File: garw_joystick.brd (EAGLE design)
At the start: 45 x 30 mm, 15 parts, among them IC1 TLC339D, X1 PS-05_WL, X2 PS-08_WL

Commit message: Improve board
Signed-off-by: Ralf Ramsauer <ralf@vmexit.de>
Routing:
- net GARW4: track 35.6 -> 37.9 mm
- net GND: track 84.9 -> 85.5 mm

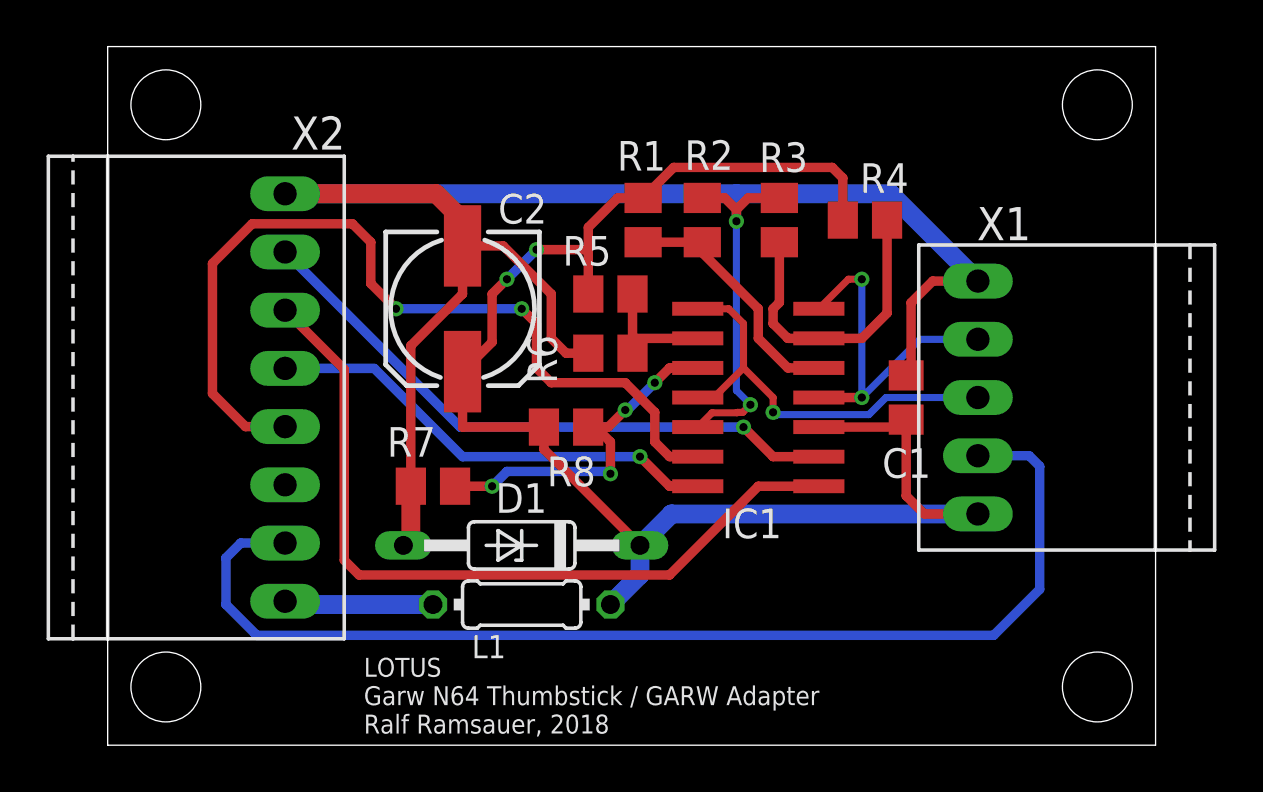
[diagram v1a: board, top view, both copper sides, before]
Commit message: Add low pass filters
Signed-off-by: Ralf Ramsauer <ralf@vmexit.de>
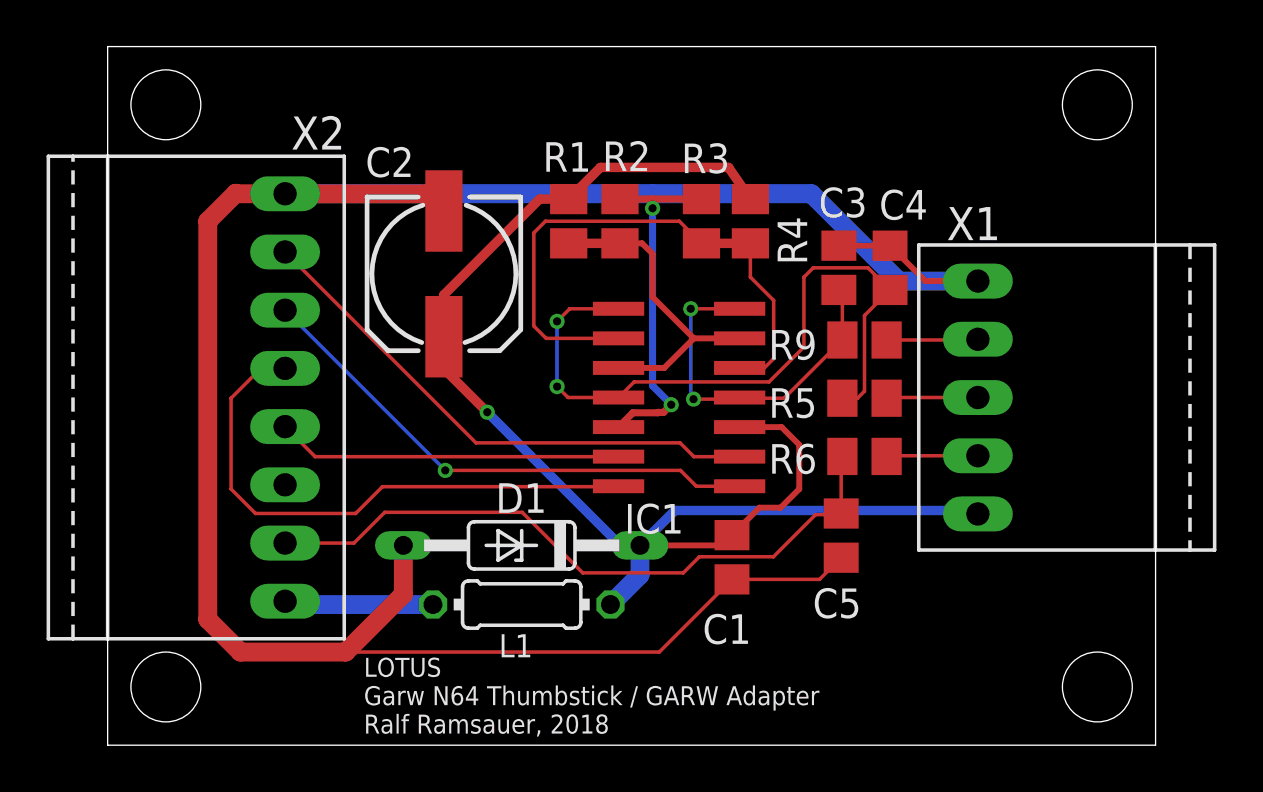
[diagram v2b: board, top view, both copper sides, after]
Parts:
- removed R7, R8: (no value), rcl:M0805
- added C3, C4, C5: 100n, rcl:C0805
- added R9: (no value), rcl:M0805
- R1, R3: value (none) -> 1k3
- R2, R4: value (none) -> 22k
- R6: value (none) -> 10k
- moved R5 11.8 mm to (32.5, 14.9)
- moved R6 11.8 mm to (32.5, 12.4), turned to 180 degrees
- moved C1 10.1 mm to (26.8, 8.07), turned to 270 degrees
- moved R4 4.92 mm to (27.6, 22.5), turned to 90 degrees
- moved R2 3.54 mm to (22.0, 22.5)
- moved IC1 3.40 mm to (24.5, 14.9)
- moved R3 3.35 mm to (25.5, 22.5)
- moved R1 3.20 mm to (19.8, 22.5)
- moved C2 1.70 mm to (14.4, 20.2)
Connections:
- removed net N$2: IC1.6, R3.2, R4.1
- removed net N$3: IC1.9, R5.1, R6.2
- removed net N$4: IC1.10, R7.2, R8.1
- new net 0V67: IC1.5, IC1.9, R3.2, R4.1
- new net 11V33: IC1.10, IC1.6, R1.1, R2.2
- new net N$5: C4.2, IC1.11, IC1.8, R5.2
- new net N$8: C3.2, IC1.4, IC1.7, R9.2
- net GARW_LAP: now also C5.2, R6.2; no longer X1.02
- net GND: now also C3.1, C4.1, C5.1; no longer R6.1, R7.1
- net JOY1: now also R9.1; no longer IC1.4, IC1.7
- net JOY2: now also R5.1; no longer IC1.11, IC1.8
- net N$1: now also R6.1, X1.02; no longer IC1.5, R1.1, R2.2
- net VCC: no longer R5.2, R8.2
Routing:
- net GND: track 85.5 -> 117.0 mm
- net N$5: track 0.00 -> 30.5 mm, vias 0 -> 2
- net 0V67: track 0.00 -> 24.8 mm
- net GARW4: track 37.9 -> 14.9 mm, vias 2 -> 0
- net GARW_LAP: track 49.3 -> 29.0 mm
- net N$8: track 0.00 -> 16.0 mm, vias 0 -> 2
- net N$4: track 15.2 -> 0.00 mm, vias 4 -> 0
- net JOY2: track 18.2 -> 3.93 mm, vias 1 -> 0
- net 11V33: track 0.00 -> 13.9 mm
- net N$2: track 13.2 -> 0.00 mm
- net JOY1: track 15.3 -> 3.93 mm, vias 2 -> 0
- net GARW2: track 34.0 -> 22.7 mm, vias 0 -> 1
- net N$1: track 10.8 -> 3.93 mm
- net N$3: track 5.34 -> 0.00 mm
- net VCC: track 67.0 -> 61.8 mm, vias 2 -> 1
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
